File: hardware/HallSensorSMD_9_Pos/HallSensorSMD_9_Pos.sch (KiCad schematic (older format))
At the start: 11 parts, among them J1 Power/Signal, U1 ATtiny814-SS, U10 Hall 8, U2 Hall 1, U3 Hall 2, U4 Hall 3, U5 Hall 4, U6 Hall 5, U7 Hall 6, U8 Hall 7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

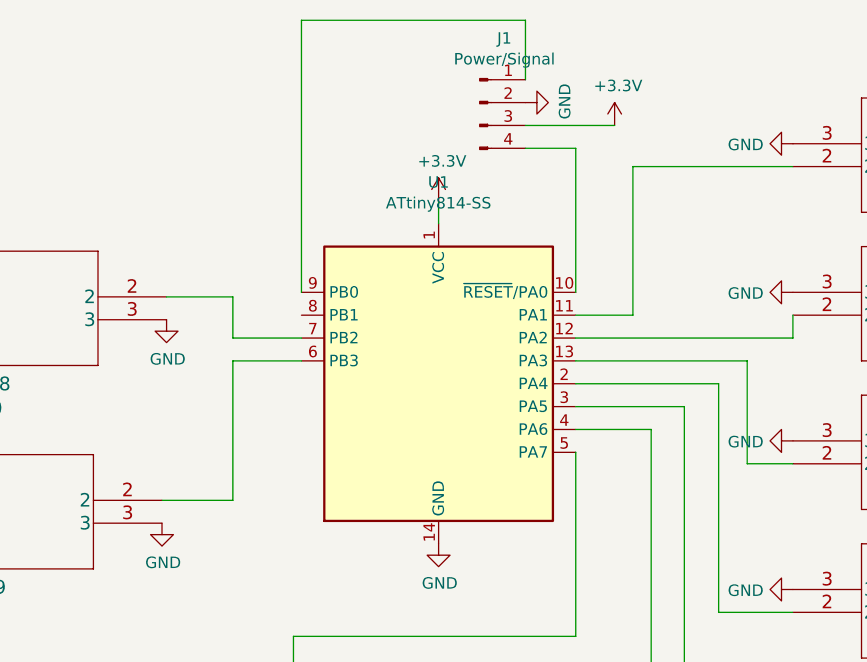
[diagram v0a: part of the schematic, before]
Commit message: updating Hall Sensor 9 Position pin assignments
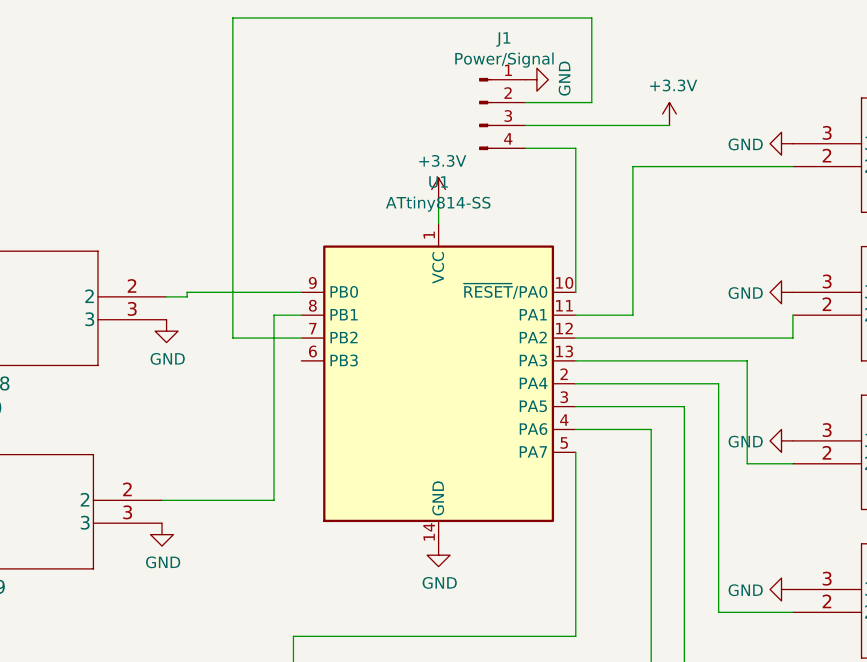
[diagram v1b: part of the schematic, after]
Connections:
- net GND: now also J1.1 (Pin_1); no longer J1.2 (Pin_2)
- net at U1.6 (PB3): no longer U9.2
- net at U1.7 (PB2): now also J1.2 (Pin_2); no longer U10.2
- net at U1.8 (PB1): now also U9.2
- net at U1.9 (PB0): now also U10.2; no longer J1.1 (Pin_1)
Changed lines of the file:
@@
 L power:+3.3V #PWR0101
 U 1 1 5F12C8E8
-P 6220 2520
-F 0 "#PWR0101" H 6220 2370 50  0001 C CNN
-F 1 "+3.3V" H 6235 2693 50  0000 C CNN
-F 2 "" H 6220 2520 50  0001 C CNN
-F 3 "" H 6220 2520 50  0001 C CNN
-	1    6220 2520
+P 6460 2520
+F 0 "#PWR0101" H 6460 2370 50  0001 C CNN
+F 1 "+3.3V" H 6475 2693 50  0000 C CNN
+F 2 "" H 6460 2520 50  0001 C CNN
+F 3 "" H 6460 2520 50  0001 C CNN
+	1    6460 2520
 	1    0    0    -1
 $EndComp
@@
 L power:GND #PWR0104
 U 1 1 601299F5
-P 5830 2420
-F 0 "#PWR0104" H 5830 2170 50  0001 C CNN
-F 1 "GND" H 5835 2247 50  0000 C CNN
-F 2 "" H 5830 2420 50  0001 C CNN
-F 3 "" H 5830 2420 50  0001 C CNN
-	1    5830 2420
+P 5830 2320
+F 0 "#PWR0104" H 5830 2070 50  0001 C CNN
+F 1 "GND" H 5835 2147 50  0000 C CNN
+F 2 "" H 5830 2320 50  0001 C CNN
+F 3 "" H 5830 2320 50  0001 C CNN
+	1    5830 2320
 	0    -1   -1   0
 $EndComp
@@
 $EndComp
 Wire Wire Line
-	5830 2520 6220 2520
-Wire Wire Line
 	6050 3250 6050 2620
 Wire Wire Line
 	6050 2620 5830 2620
-Wire Wire Line
-	4850 3250 4850 2060
-Wire Wire Line
-	4850 2060 5830 2060
-Wire Wire Line
-	5830 2060 5830 2320
 $Comp
 L 2020-06-24_03-37-49:SS49E U9
@@
 $EndComp
 Wire Wire Line
-	4260 3270 4550 3270
-Wire Wire Line
-	4550 3270 4550 3450
-Wire Wire Line
-	4550 3450 4850 3450
-Wire Wire Line
-	4240 4160 4550 4160
-Wire Wire Line
-	4550 4160 4550 3550
-Wire Wire Line
-	4550 3550 4850 3550
+	4850 3450 4550 3450
+Wire Wire Line
+	4550 3450 4550 2050
+Wire Wire Line
+	4550 2050 6120 2050
+Wire Wire Line
+	4850 3250 4350 3250
+Wire Wire Line
+	4350 3250 4350 3270
+Wire Wire Line
+	4350 3270 4260 3270
+Wire Wire Line
+	4240 4160 4730 4160
+Wire Wire Line
+	4730 4160 4730 3350
+Wire Wire Line
+	4730 3350 4850 3350
+Wire Wire Line
+	5830 2520 6460 2520
+Wire Wire Line
+	6120 2050 6120 2420
+Wire Wire Line
+	6120 2420 5830 2420
 $EndSCHEMATC

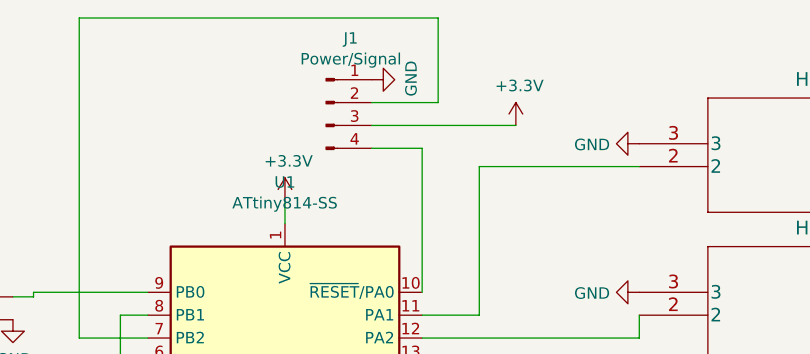
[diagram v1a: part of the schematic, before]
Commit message: gerbers for HallSensor and InputBoard PCBs, updates to HallSensor PCBs
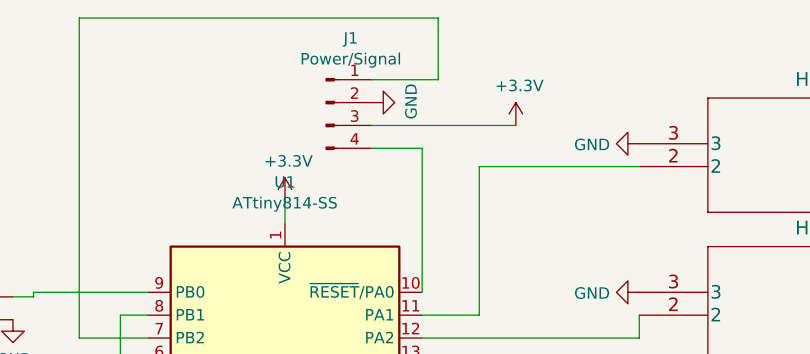
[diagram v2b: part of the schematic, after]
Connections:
- net GND: now also J1.2 (Pin_2); no longer J1.1 (Pin_1)
- net at U1.7 (PB2): now also J1.1 (Pin_1); no longer J1.2 (Pin_2)
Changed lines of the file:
@@
 L power:GND #PWR0104
 U 1 1 601299F5
-P 5830 2320
-F 0 "#PWR0104" H 5830 2070 50  0001 C CNN
-F 1 "GND" H 5835 2147 50  0000 C CNN
-F 2 "" H 5830 2320 50  0001 C CNN
-F 3 "" H 5830 2320 50  0001 C CNN
-	1    5830 2320
+P 5830 2420
+F 0 "#PWR0104" H 5830 2170 50  0001 C CNN
+F 1 "GND" H 5835 2247 50  0000 C CNN
+F 2 "" H 5830 2420 50  0001 C CNN
+F 3 "" H 5830 2420 50  0001 C CNN
+	1    5830 2420
 	0    -1   -1   0
 $EndComp
@@
 	5830 2520 6460 2520
 Wire Wire Line
-	6120 2050 6120 2420
-Wire Wire Line
-	6120 2420 5830 2420
+	5830 2320 6120 2320
+Wire Wire Line
+	6120 2320 6120 2050
 $EndSCHEMATC
